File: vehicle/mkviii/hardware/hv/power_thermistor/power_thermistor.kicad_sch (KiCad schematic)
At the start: 2 parts, among them J2 J_Molex_Header_01x02_VT, U1 DS18B20U

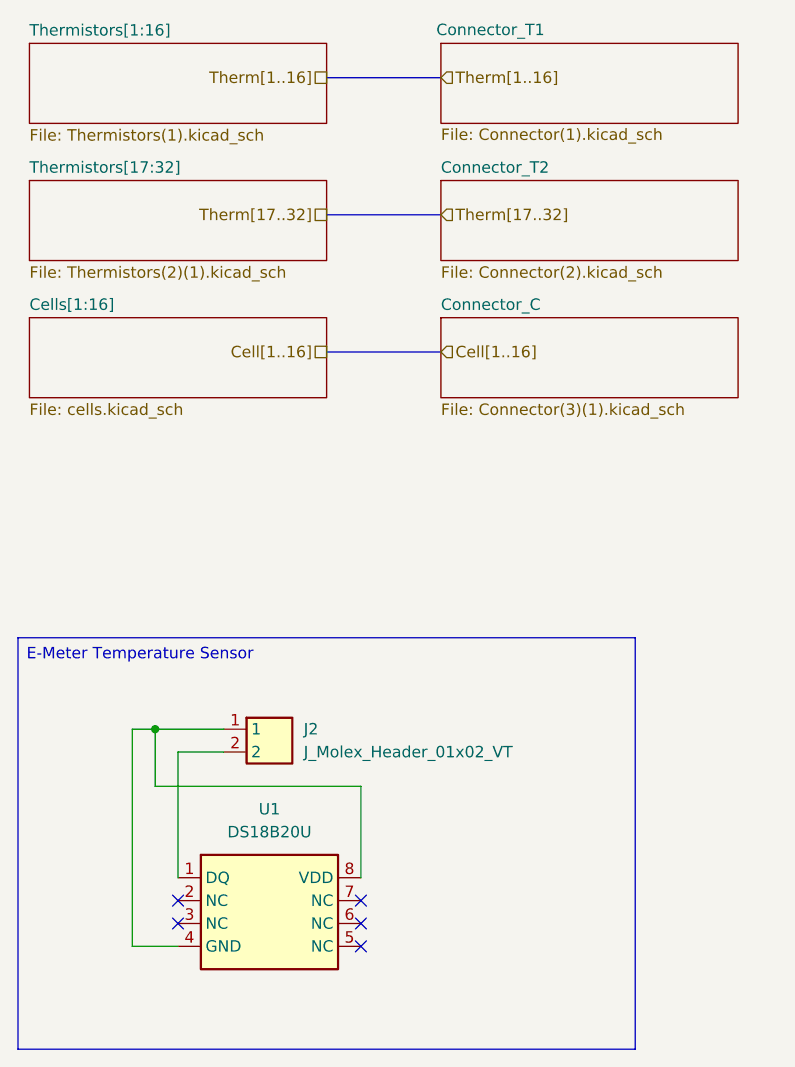
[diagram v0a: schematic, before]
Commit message: Power Therm overhall, have not been reviewed yet
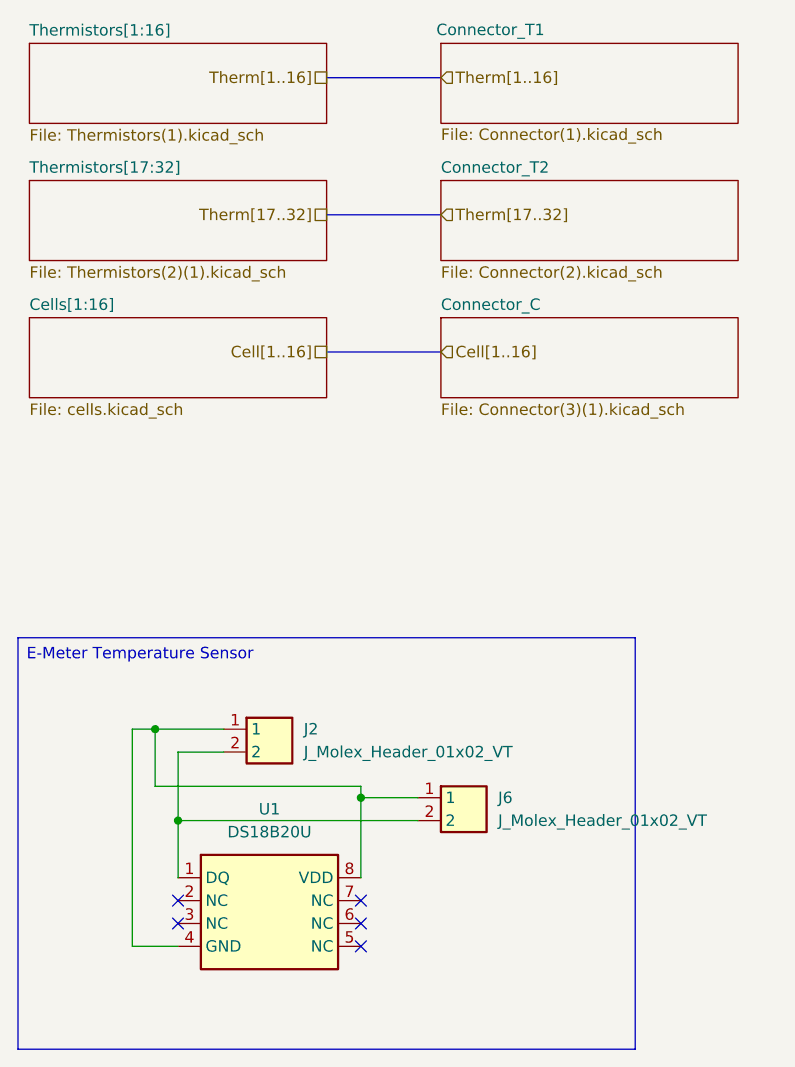
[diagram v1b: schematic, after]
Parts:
- added J6: J_Molex_Header_01x02_VT, OEM:J_Molex_Header_01x02_VT - 43045-02YY_121314, symbol OEM:J_Molex_Header_01x02_VT
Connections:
- net at J2.2, U1.1 (DQ): now also J6.2
- net at J2.1, U1.4 (GND), U1.8 (VDD): now also J6.1
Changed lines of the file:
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@@
+		(color 0 0 0 0)
+	)
+	(junction
+		(at 59.69 139.7)
+		(diameter 0)
+		(color 0 0 0 0)
+	)
+	(junction
+		(at 80.01 137.16)
+		(diameter 0)
 		(color 0 0 0 0)
 	)
@@
 	(wire
 		(pts
+			(xy 59.69 139.7) (xy 86.36 139.7)
+		)
+		(stroke
+			(width 0)
+			(type default)
+		)
+	)
+	(wire
+		(pts
 			(xy 59.69 153.67) (xy 54.61 153.67)
 		)
@@
 	(wire
 		(pts
-			(xy 59.69 132.08) (xy 59.69 146.05)
+			(xy 59.69 132.08) (xy 59.69 139.7)
 		)
 		(stroke
@@
 	(wire
 		(pts
-			(xy 80.01 146.05) (xy 80.01 135.89)
+			(xy 80.01 146.05) (xy 80.01 137.16)
+		)
+		(stroke
+			(width 0)
+			(type default)
+		)
+	)
+	(wire
+		(pts
+			(xy 59.69 139.7) (xy 59.69 146.05)
+		)
+		(stroke
+			(width 0)
+			(type default)
+		)
+	)
+	(wire
+		(pts
+			(xy 80.01 137.16) (xy 80.01 135.89)
 		)
 		(stroke
@@
 		(pts
 			(xy 57.15 135.89) (xy 57.15 129.54)
+		)
+		(stroke
+			(width 0)
+			(type default)
+		)
+	)
+	(wire
+		(pts
+			(xy 80.01 137.16) (xy 86.36 137.16)
 		)
 		(stroke
@@
 					(unit 1)
 				)
+			)
+		)
+	)
+	(symbol
+		(lib_id "OEM:J_Molex_Header_01x02_VT")
+		(at 91.44 138.43 0)
+		(unit 1)
+		(exclude_from_sim no)
+		(in_bom yes)
+		(on_board yes)
+		(dnp no)
+		(fields_autoplaced yes)
+		(property "Reference" "J6"
+			(at 95.25 137.1599 0)
+			(effects
+				(font
+					(size 1.27 1.27)
+				)
+				(justify left)
+			)
+		)
+		(property "Value" "J_Molex_Header_01x02_VT"
+			(at 95.25 139.6999 0)
+			(effects
+				(font
+					(size 1.27 1.27)
+				)
+				(justify left)
+			)
+		)
+		(property "Footprint" "OEM:J_Molex_Header_01x02_VT - 43045-02YY_121314"
+			(at 107.95 233.35 0)
+			(effects
+				(font
+					(size 1.27 1.27)
+				)
+				(justify left top)
+				(hide yes)
+			)
+		)
+		(property "Datasheet" "https://www.molex.com/pdm_docs/sd/430450612_sd.pdf"
+			(at 107.95 333.35 0)
+			(effects
+				(font
+					(size 1.27 1.27)
+				)
+				(justify left top)
+				(hide yes)
+			)
+		)
+		(property "Description" "CONN HEADER VERT 2POS"
+			(at 82.55 137.16 0)
+			(effects
+				(font
+					(size 1.27 1.27)
+				)
+				(hide yes)
+			)
+		)
+		(property "MPN" "43045-0212"
+			(at 107.95 933.35 0)
+			(effects
+				(font
+					(size 1.27 1.27)
+				)
+				(justify left top)
+				(hide yes)
+			)
+		)
+		(pin "2"
+		)
+		(pin "1"
+		)
+		(instances
+			(project "power_thermistor"
+				(path "/9871410e-0b94-49cd-ba7d-079975b9e567"
+					(reference "J6")
+					(unit 1)
+				)
